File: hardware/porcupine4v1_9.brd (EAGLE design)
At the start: 24.4 x 27.4 mm, 33 parts, among them X1 PROGCON

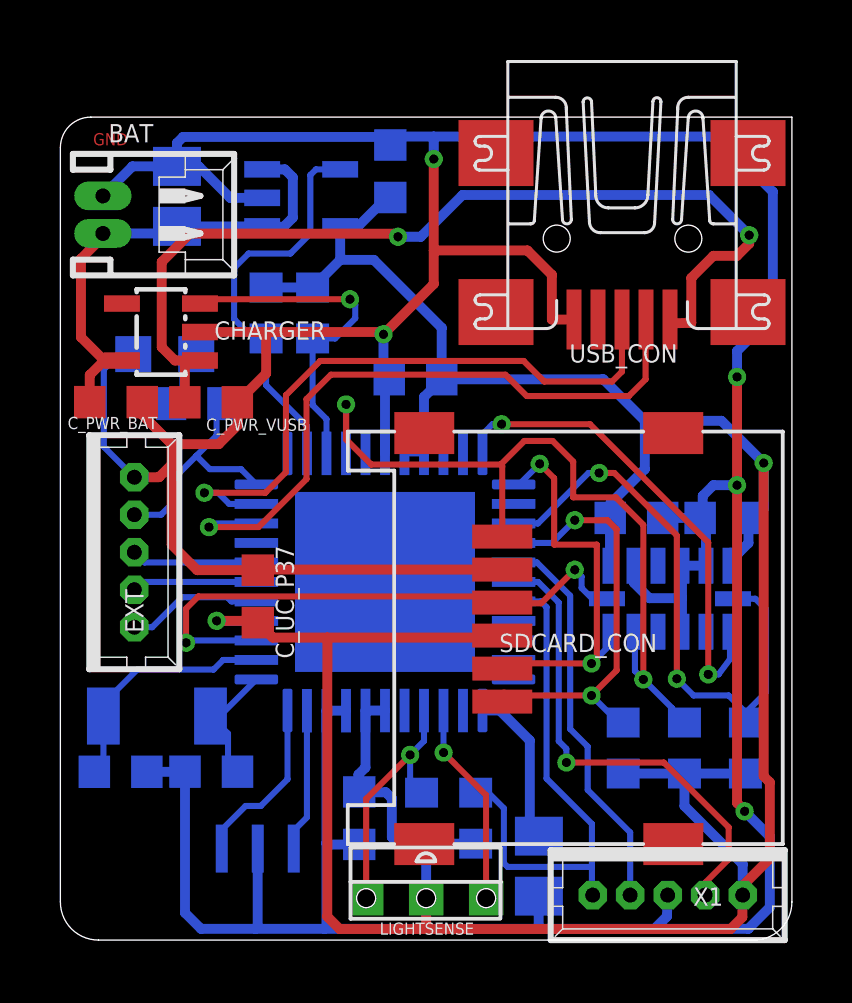
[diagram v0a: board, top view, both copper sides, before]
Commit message: updated hedgehog library and next iteration versions
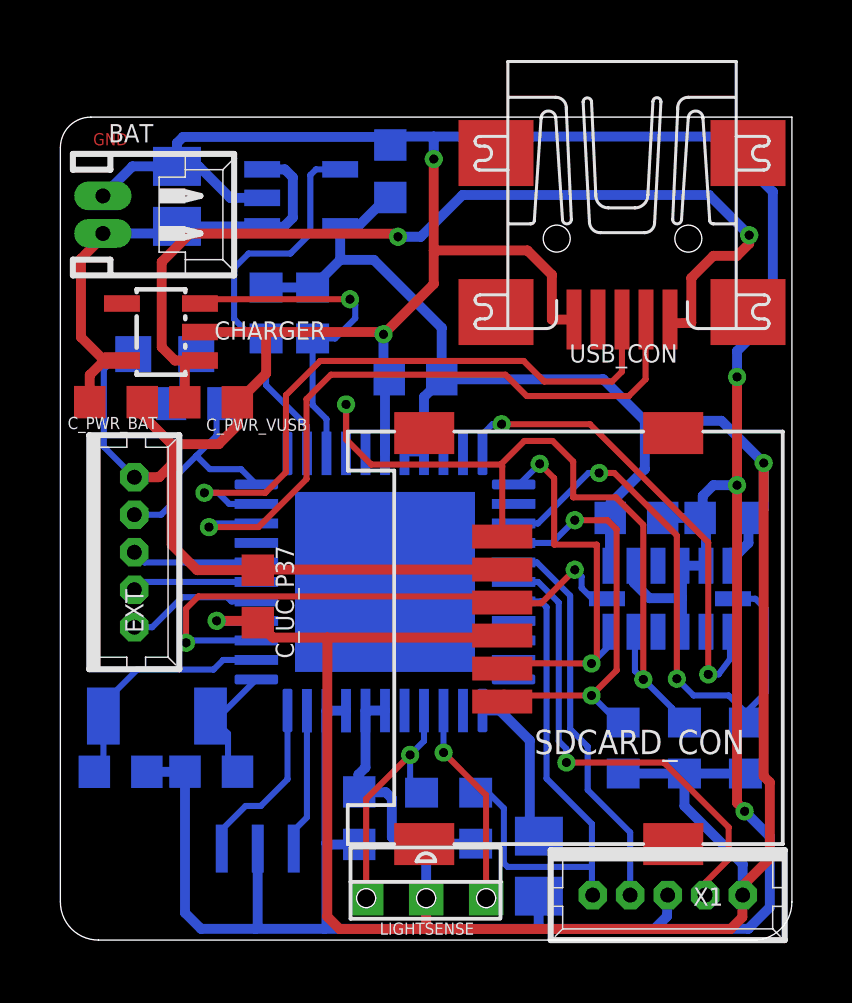
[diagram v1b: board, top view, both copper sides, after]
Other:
- board text removed: "SDCARD_CON"
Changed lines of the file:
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@@
 <grid distance="1" unitdist="mil" unit="mil" style="dots" multiple="10" display="yes" altdistance="1" altunitdist="mil" altunit="mil"/>
 <layers>
-<layer number="1" name="Top" color="4" fill="1" visible="yes" active="yes"/>
-<layer number="16" name="Bottom" color="1" fill="1" visible="yes" active="yes"/>
-<layer number="17" name="Pads" color="2" fill="1" visible="yes" active="yes"/>
-<layer number="18" name="Vias" color="2" fill="1" visible="yes" active="yes"/>
-<layer number="19" name="Unrouted" color="6" fill="1" visible="yes" active="yes"/>
+<layer number="1" name="Top" color="4" fill="1" visible="no" active="yes"/>
+<layer number="16" name="Bottom" color="1" fill="1" visible="no" active="yes"/>
+<layer number="17" name="Pads" color="2" fill="1" visible="no" active="yes"/>
+<layer number="18" name="Vias" color="2" fill="1" visible="no" active="yes"/>
+<layer number="19" name="Unrouted" color="6" fill="1" visible="no" active="yes"/>
 <layer number="20" name="Dimension" color="15" fill="1" visible="yes" active="yes"/>
 <layer number="21" name="tPlace" color="7" fill="1" visible="yes" active="yes"/>
-<layer number="22" name="bPlace" color="7" fill="1" visible="yes" active="yes"/>
+<layer number="22" name="bPlace" color="7" fill="1" visible="no" active="yes"/>
 <layer number="23" name="tOrigins" color="15" fill="1" visible="yes" active="yes"/>
-<layer number="24" name="bOrigins" color="15" fill="1" visible="yes" active="yes"/>
-<layer number="25" name="tNames" color="7" fill="1" visible="no" active="yes"/>
+<layer number="24" name="bOrigins" color="15" fill="1" visible="no" active="yes"/>
+<layer number="25" name="tNames" color="7" fill="1" visible="yes" active="yes"/>
 <layer number="26" name="bNames" color="7" fill="1" visible="no" active="yes"/>
 <layer number="27" name="tValues" color="7" fill="1" visible="no" active="yes"/>
@@
 <layer number="47" name="Measures" color="7" fill="1" visible="no" active="yes"/>
 <layer number="48" name="Document" color="7" fill="1" visible="yes" active="yes"/>
-<layer number="49" name="Reference" color="7" fill="1" visible="no" active="yes"/>
+<layer number="49" name="Reference" color="7" fill="1" visible="yes" active="yes"/>
 <layer number="50" name="dxf" color="7" fill="1" visible="no" active="yes"/>
 <layer number="51" name="tDocu" color="7" fill="1" visible="yes" active="yes"/>
-<layer number="52" name="bDocu" color="7" fill="1" visible="yes" active="yes"/>
+<layer number="52" name="bDocu" color="7" fill="1" visible="no" active="yes"/>
 <layer number="53" name="tGND_GNDA" color="7" fill="9" visible="no" active="no"/>
 <layer number="54" name="bGND_GNDA" color="1" fill="9" visible="no" active="no"/>
@@
 <wire x1="23.114" y1="0" x2="1.27" y2="0" width="0.0254" layer="20"/>
 <text x="1.0922" y="26.4922" size="0.4064" layer="1" font="vector" ratio="15">GND</text>
-<text x="14.6304" y="9.6012" size="0.6096" layer="25">SDCARD_CON</text>
 <text x="8.3566" y="1.4732" size="0.4064" layer="26" rot="MR0">12MHZ_RESONATOR</text>
 <text x="5.3086" y="8.4328" size="0.4064" layer="26" rot="MR0">32KHZ_CRYSTAL</text>
@@
 </autorouter>
 <elements>
-<element name="SDCARD_CON" library="HedgehogLib" package="460DA40013" value="MICROSD_CONN" x="24.0792" y="3.2004" rot="R180"/>
+<element name="SDCARD_CON" library="HedgehogLib" package="460DA40013" value="MICROSD_CONN" x="24.0792" y="3.2004" smashed="yes" rot="R180">
+<attribute name="VALUE" x="22.8092" y="14.6304" size="1.016" layer="27" rot="R180"/>
+<attribute name="NAME" x="22.8092" y="7.0104" size="0.8128" layer="25" rot="R180"/>
+</element>
 <element name="LIGHTSENSE" library="HedgehogLib" package="TSL" value="TSL250" x="12.192" y="1.397" rot="R180"/>
 <element name="USB_CON" library="HedgehogLib" package="248601" value="USBCON" x="18.7216" y="22.9344" smashed="yes" rot="R270">
